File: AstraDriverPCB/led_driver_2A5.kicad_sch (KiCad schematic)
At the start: 7 parts, among them U2 LED2001PHR

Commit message: progress
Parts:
- removed C4: 22u, LiveAstra:C_0603_1608Metric, symbol LiveAstra:C_22uF_X5R_0603
- added C1: 22u, LiveAstra:C_0805_2012Metric_Pad1.18x1.45mm_HandSolder, symbol LiveAstra:C_22uF_X5R_0805
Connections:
- net +5V: now also C1.2
- net GND: now also C1.1
- net SW_OUT: now reaches L2.1, U2.7 (SW)
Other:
- moved on the sheet: C13, L2

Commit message: Finished layout
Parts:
- renumbered C13 to C14, C2 to C3, C1 to C4
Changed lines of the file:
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@@
 		(dnp no)
 		(fields_autoplaced yes)
-		(property "Reference" "C2"
+		(property "Reference" "C3"
 			(at 107.95 107.3149 90)
 			(effects
@@
 		(dnp no)
 		(fields_autoplaced yes)
-		(property "Reference" "C13"
+		(property "Reference" "C14"
 			(at 205.74 69.2149 90)
 			(effects
@@
 		(dnp no)
 		(fields_autoplaced yes)
-		(property "Reference" "C1"
+		(property "Reference" "C4"
 			(at 107.95 60.9599 90)
 			(effects

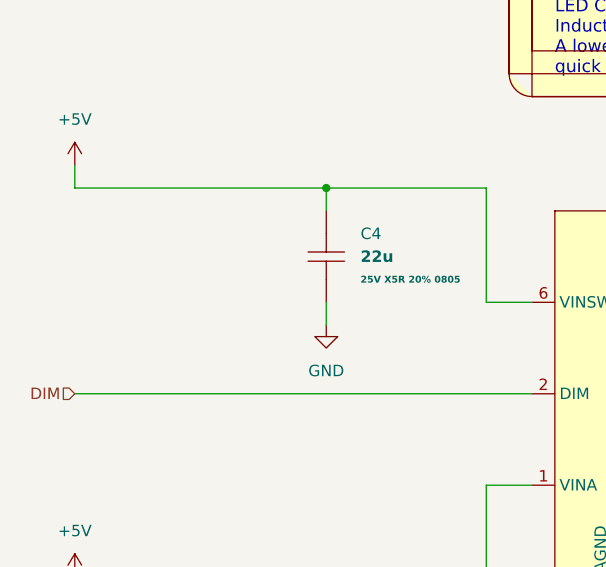
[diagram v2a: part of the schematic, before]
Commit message: Added extra caps, cleanup
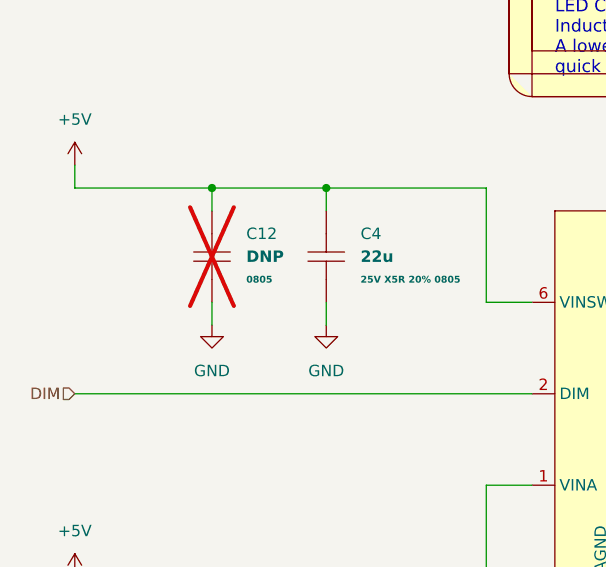
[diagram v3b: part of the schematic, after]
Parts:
- added C12: DNP, LiveAstra:C_DNP_0805_2012Metric_Pad1.18x1.45mm_HandSolder, symbol LiveAstra:C_DNP_0805
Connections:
- net +5V: now also C12.2
- net GND: now also C12.1
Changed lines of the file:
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@@
 	)
 	(junction
+		(at 91.44 55.88)
+		(diameter 0)
+		(color 0 0 0 0)
+	)
+	(junction
 		(at 218.44 88.9)
 		(diameter 0)
@@
 	(wire
 		(pts
-			(xy 76.2 55.88) (xy 104.14 55.88)
+			(xy 76.2 55.88) (xy 91.44 55.88)
 		)
 		(stroke
@@
 	(wire
 		(pts
+			(xy 91.44 55.88) (xy 104.14 55.88)
+		)
+		(stroke
+			(width 0)
+			(type default)
+		)
+	)
+	(wire
+		(pts
 			(xy 154.94 101.6) (xy 154.94 104.14)
 		)
@@
 	(wire
 		(pts
+			(xy 91.44 71.12) (xy 91.44 68.58)
+		)
+		(stroke
+			(width 0)
+			(type default)
+		)
+	)
+	(wire
+		(pts
 			(xy 121.92 101.6) (xy 121.92 88.9)
 		)
@@
 	(wire
 		(pts
+			(xy 91.44 55.88) (xy 91.44 58.42)
+		)
+		(stroke
+			(width 0)
+			(type default)
+		)
+	)
+	(wire
+		(pts
 			(xy 201.93 63.5) (xy 201.93 66.04)
 		)
@@
 	)
 	(symbol
+		(lib_id "power:GND")
+		(at 91.44 71.12 0)
+		(unit 1)
+		(exclude_from_sim no)
+		(in_bom yes)
+		(on_board yes)
+		(dnp no)
+		(fields_autoplaced yes)
+		(property "Reference" "#PWR043"
+			(at 91.44 77.47 0)
+			(effects
+				(font
+					(size 1.27 1.27)
+				)
+				(hide yes)
+			)
+		)
+		(property "Value" "GND"
+			(at 91.44 76.2 0)
+			(effects
+				(font
+					(size 1.27 1.27)
+				)
+			)
+		)
+		(property "Footprint" ""
+			(at 91.44 71.12 0)
+			(effects
+				(font
+					(size 1.27 1.27)
+				)
+				(hide yes)
+			)
+		)
+		(property "Datasheet" ""
+			(at 91.44 71.12 0)
+			(effects
+				(font
+					(size 1.27 1.27)
+				)
+				(hide yes)
+			)
+		)
+		(property "Description" "Power symbol creates a global label with name \"GND\" , ground"
+			(at 91.44 71.12 0)
+			(effects
+				(font
+					(size 1.27 1.27)
+				)
+				(hide yes)
+			)
+		)
+		(pin "1"
+		)
+		(instances
+			(project "AstraDriver"
+				(path "/d8760d88-6646-4dd8-a980-02e776803cc5/db9d16fd-00a9-4695-9dd4-6de80f9e2ffc/2917a49e-0b0c-4bc9-a147-180770b18779"
+					(reference "#PWR044")
+					(unit 1)
+				)
+				(path "/d8760d88-6646-4dd8-a980-02e776803cc5/db9d16fd-00a9-4695-9dd4-6de80f9e2ffc/5a9ee1ee-cc67-48b8-9e13-71946b2dc8ce"
+					(reference "#PWR045")
+					(unit 1)
+				)
+				(path "/d8760d88-6646-4dd8-a980-02e776803cc5/db9d16fd-00a9-4695-9dd4-6de80f9e2ffc/e6bfebdf-aa19-4866-bf09-731e468084aa"
+					(reference "#PWR043")
+					(unit 1)
+				)
+			)
+		)
+	)
+	(symbol
 		(lib_id "power:+5V")
 		(at 76.2 53.34 0)
@@
 					(unit 1)
 				)
+			)
+		)
+	)
+	(symbol
+		(lib_id "LiveAstra:C_DNP_0805")
+		(at 91.44 63.5 90)
+		(unit 1)
+		(exclude_from_sim no)
+		(in_bom no)
+		(on_board yes)
+		(dnp yes)
+		(fields_autoplaced yes)
+		(property "Reference" "C12"
+			(at 95.25 60.9599 90)
+			(effects
+				(font
+					(size 1.27 1.27)
+				)
+				(justify right)
+			)
+		)
+		(property "Value" "DNP"
+			(at 95.25 63.5 90)
+			(effects
+				(font
+					(size 1.27 1.27)
+					(bold yes)
+				)
+				(justify right)
+			)
+		)
+		(property "Footprint" "LiveAstra:C_DNP_0805_2012Metric_Pad1.18x1.45mm_HandSolder"
+			(at 100.33 63.5 0)
+			(effects
+				(font
+					(size 1.27 1.27)
+				)
+				(hide yes)
+			)
+		)
+		(property "Datasheet" ""
+			(at 104.14 63.5 0)
+			(effects
+				(font
+					(size 1.27 1.27)
+				)
+				(hide yes)
+			)
+		)
+		(property "Description" "DNP"
+			(at 96.52 63.5 0)
+			(effects
+				(font
+					(size 1.27 1.27)
+				)
+				(hide yes)
+			)
+		)
+		(property "LCSC Part" ""
+			(at 107.95 63.5 0)
+			(effects
+				(font
+					(size 1.27 1.27)
+				)
+				(hide yes)
+			)
+		)
+		(property "Extra Values" "0805"
+			(at 95.25 66.0399 90)
+			(effects
+				(font
+					(size 0.762 0.762)
+					(bold yes)
+				)
+				(justify right)
+			)
+		)
+		(pin "1"
+		)
+		(pin "2"
+		)
+		(instances
+			(project "AstraDriver"
+				(path "/d8760d88-6646-4dd8-a980-02e776803cc5/db9d16fd-00a9-4695-9dd4-6de80f9e2ffc/2917a49e-0b0c-4bc9-a147-180770b18779"
+					(reference "C16")
+					(unit 1)
+				)
+				(path "/d8760d88-6646-4dd8-a980-02e776803cc5/db9d16fd-00a9-4695-9dd4-6de80f9e2ffc/5a9ee1ee-cc67-48b8-9e13-71946b2dc8ce"
+					(reference "C17")
+					(unit 1)
+				)
+				(path "/d8760d88-6646-4dd8-a980-02e776803cc5/db9d16fd-00a9-4695-9dd4-6de80f9e2ffc/e6bfebdf-aa19-4866-bf09-731e468084aa"
+					(reference "C12")
+					(unit 1)
+				)

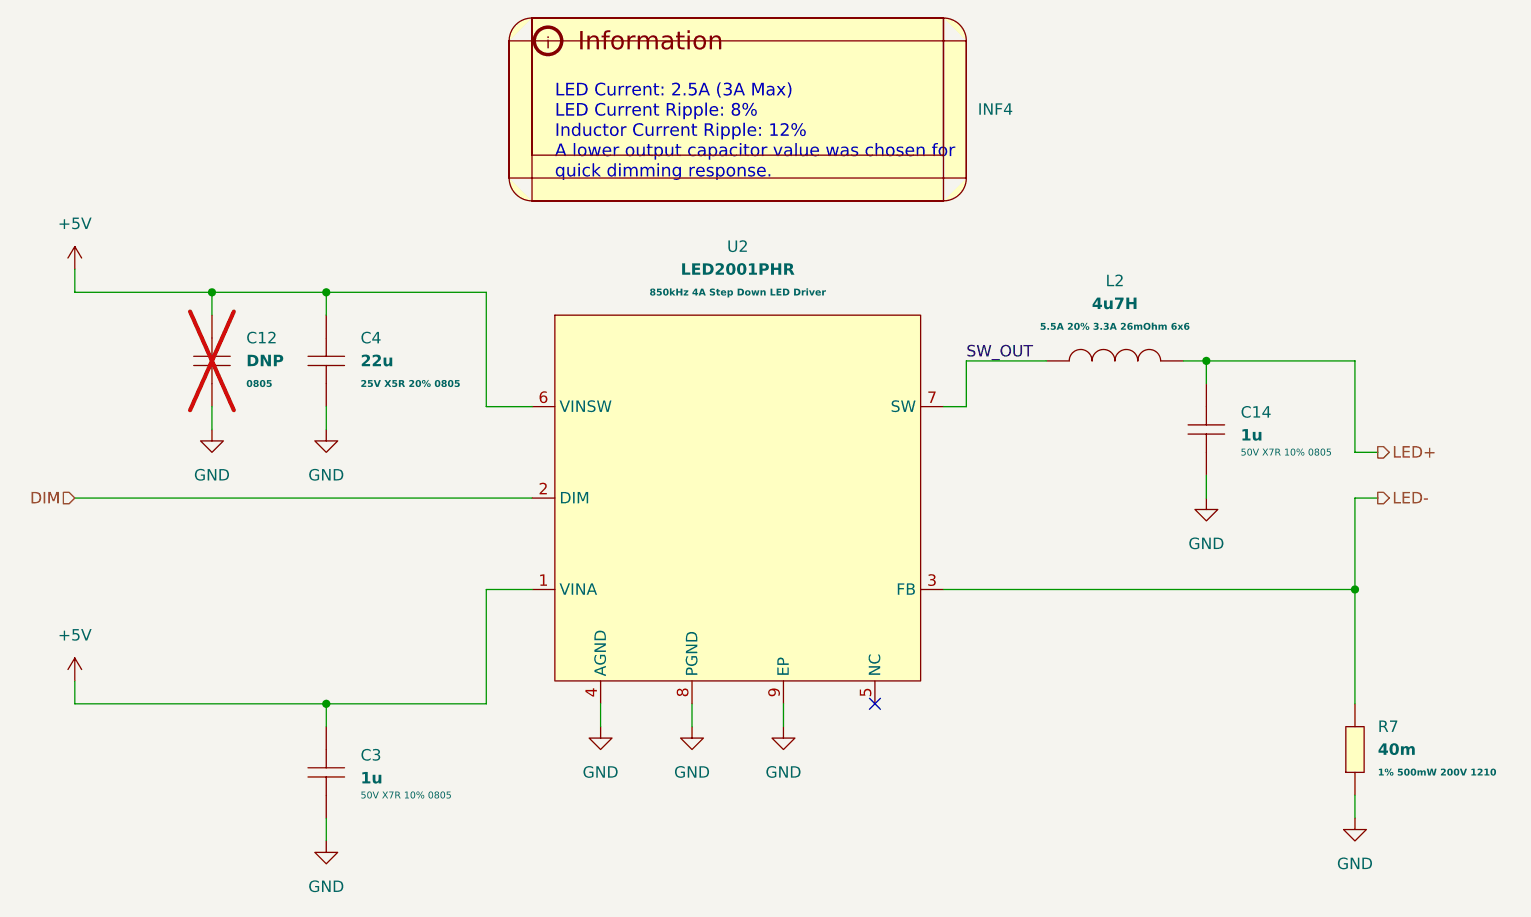
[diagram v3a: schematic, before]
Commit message: Finished silkscreen and board
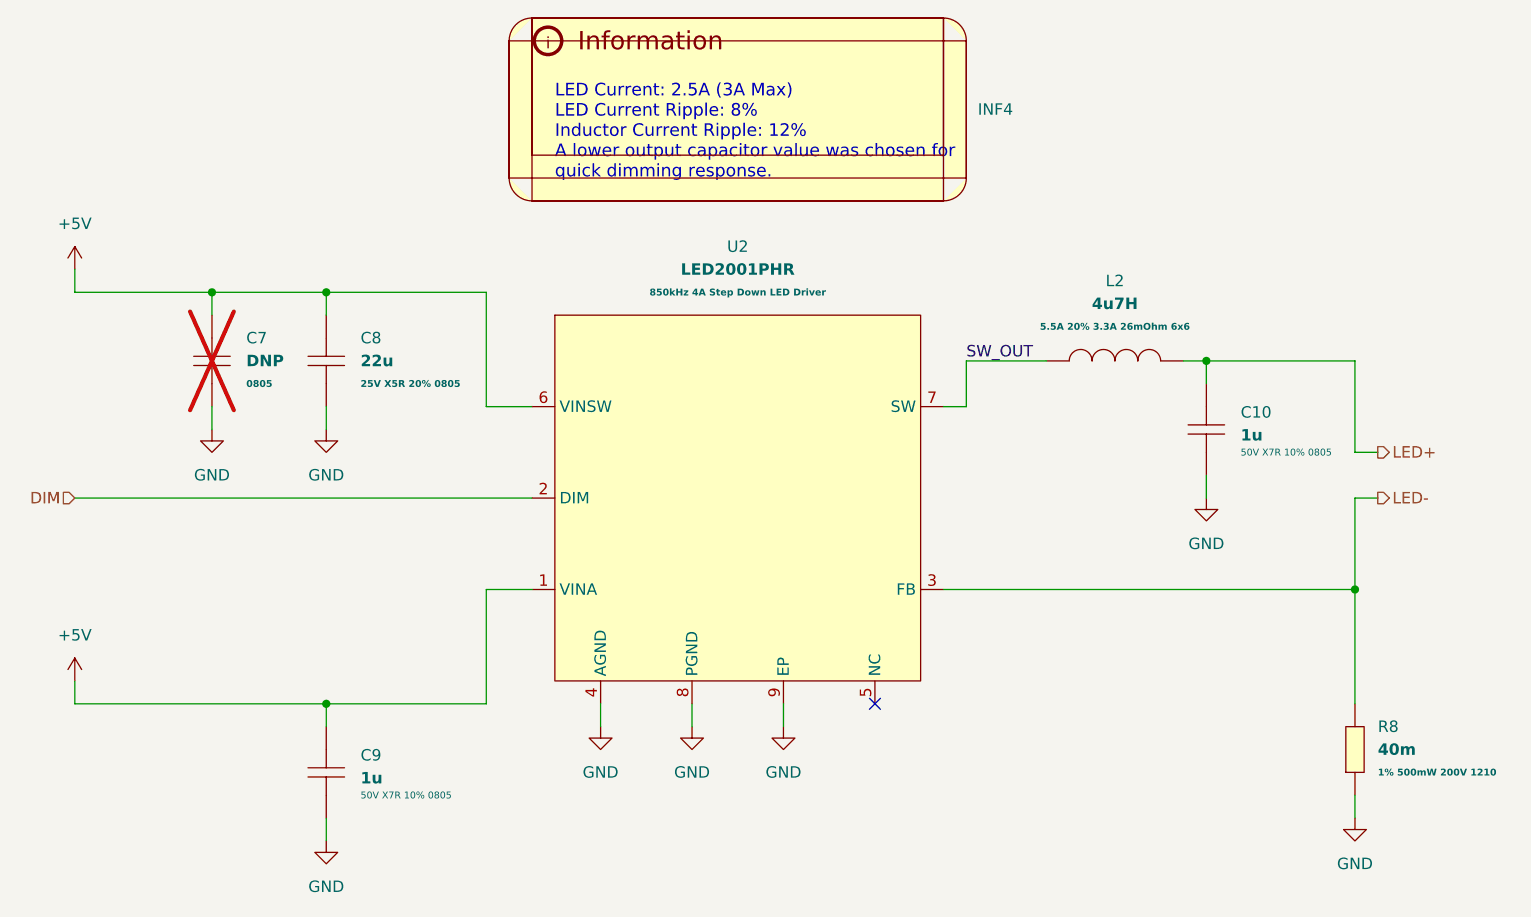
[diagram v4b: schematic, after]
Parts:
- renumbered C14 to C10, C12 to C7, C4 to C8, C3 to C9, R7 to R8
